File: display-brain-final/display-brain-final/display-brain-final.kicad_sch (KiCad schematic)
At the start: 25 parts, among them J1 Conn_01x02_Socket, J2 Conn_01x05_Socket, J3 Conn_01x19_Socket, J4 Conn_01x19_Socket, J5 Conn_01x04_Socket, J6 Conn_01x05_Socket, J7 Conn_01x02_Socket, P1 USB_C_Plug_USB2.0, U2 ESP32-WROOM-32, U3 LM317_TO-252

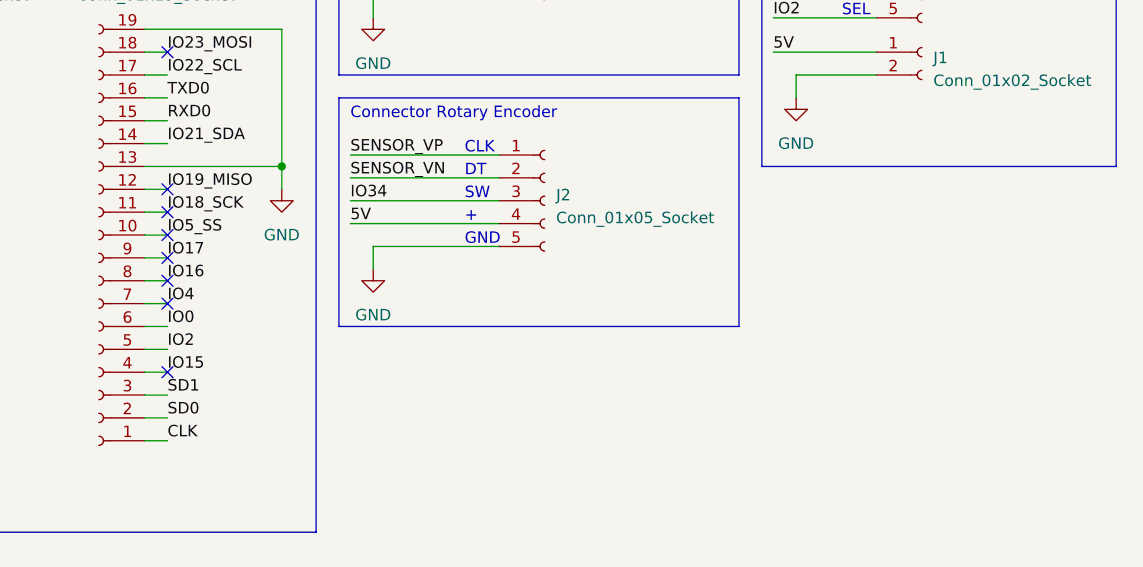
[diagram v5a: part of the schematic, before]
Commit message: display and funk changed
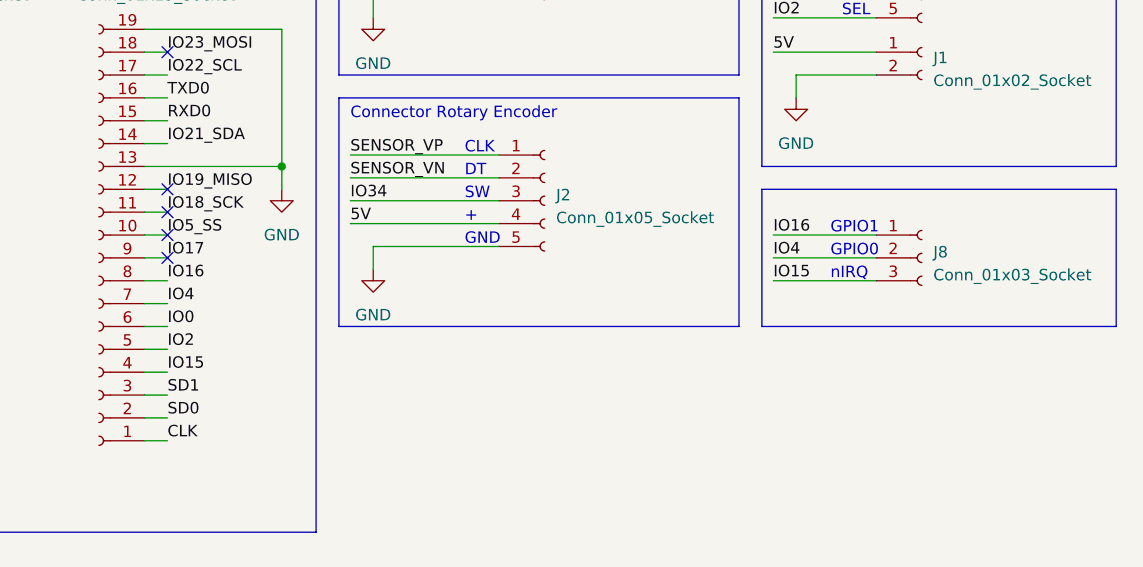
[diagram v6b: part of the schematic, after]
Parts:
- added J8: Conn_01x03_Socket, Connector_PinSocket_2.54mm:PinSocket_1x03_P2.54mm_Vertical, symbol Connector:Conn_01x03_Socket
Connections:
- net IO15: now also J8.3 (Pin_3)
- net IO16: now also J8.1 (Pin_1)
- net IO4: now also J8.2 (Pin_2)
- no-connect marks 29 -> 26
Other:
- note added: "GPIO0"
- note added: "GPIO1"
- note added: "nIRQ"
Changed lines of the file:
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@@
   (junction (at 144.78 163.83) (diameter 0) (color 0 0 0 0)
   )
-  (no_connect (at 127 59.69))
   (no_connect (at 127 54.61))
   (no_connect (at 87.63 44.45))
@@
   (no_connect (at 69.85 142.24))
   (no_connect (at 127 57.15))
-  (no_connect (at 127 62.23))
   (no_connect (at 127 49.53))
   (no_connect (at 87.63 62.23))
@@
   (no_connect (at 87.63 69.85))
   (no_connect (at 96.52 102.87))
-  (no_connect (at 127 69.85))
   (no_connect (at 83.82 102.87))
   (no_connect (at 123.19 102.87))
@@
     (stroke (width 0) (type default))
   )
+  (polyline (pts (xy 193.04 64.77) (xy 232.41 64.77))
+    (stroke (width 0) (type default))
+  )
   (wire (pts (xy 194.31 20.32) (xy 205.74 20.32))
     (stroke (width 0) (type default))
@@
     (stroke (width 0) (type default))
   )
+  (polyline (pts (xy 232.41 64.77) (xy 232.41 49.53))
+    (stroke (width 0) (type default))
+  )
   (wire (pts (xy 124.46 34.29) (xy 127 34.29))
     (stroke (width 0) (type default))
@@
     (stroke (width 0) (type default))
   )
+  (polyline (pts (xy 232.41 49.53) (xy 193.04 49.53))
+    (stroke (width 0) (type default))
+  )
   (wire (pts (xy 87.63 46.99) (xy 100.33 46.99))
     (stroke (width 0) (type default))
   )
+  (polyline (pts (xy 193.04 49.53) (xy 193.04 64.77))
+    (stroke (width 0) (type default))
+  )
   (wire (pts (xy 19.05 124.46) (xy 19.05 129.54))
     (stroke (width 0) (type default))
@@
     (stroke (width 0) (type default))
   )
+  (wire (pts (xy 194.31 54.61) (xy 205.74 54.61))
+    (stroke (width 0) (type default))
+  )
   (wire (pts (xy 59.69 34.29) (xy 66.04 34.29))
     (stroke (width 0) (type default))
@@
     (stroke (width 0) (type default))
   )
+  (wire (pts (xy 194.31 59.69) (xy 205.74 59.69))
+    (stroke (width 0) (type default))
+  )
   (wire (pts (xy 147.32 48.26) (xy 163.83 48.26))
     (stroke (width 0) (type default))
@@
     (stroke (width 0) (type default))
   )
+  (wire (pts (xy 194.31 57.15) (xy 205.74 57.15))
+    (stroke (width 0) (type default))
+  )
   (polyline (pts (xy 135.89 104.14) (xy 81.28 104.14))
     (stroke (width 0) (type default))
@@
     (effects (font (size 1.27 1.27)) (justify left bottom))
   )
+  (text "GPIO1" (at 200.66 54.61 0)
+    (effects (font (size 1.27 1.27)) (justify left bottom))
+  )
   (text "GND" (at 160.02 55.88 0)
     (effects (font (size 1.27 1.27)) (justify left bottom))
@@
   )
   (text "Power Connector" (at 15.24 111.76 0)
+    (effects (font (size 1.27 1.27)) (justify left bottom))
+  )
+  (text "GPIO0" (at 200.66 57.15 0)
+    (effects (font (size 1.27 1.27)) (justify left bottom))
+  )
+  (text "nIRQ" (at 200.66 59.69 0)
     (effects (font (size 1.27 1.27)) (justify left bottom))
   )
@@
     (effects (font (size 1.27 1.27)) (justify left bottom))
   )
+  (label "IO4" (at 194.31 57.15 0) (fields_autoplaced)
+    (effects (font (size 1.27 1.27)) (justify left bottom))
+  )
   (label "IO34" (at 147.32 50.8 0) (fields_autoplaced)
     (effects (font (size 1.27 1.27)) (justify left bottom))
@@
     (effects (font (size 1.27 1.27)) (justify left bottom))
   )
+  (label "IO16" (at 194.31 54.61 0) (fields_autoplaced)
+    (effects (font (size 1.27 1.27)) (justify left bottom))
+  )
   (label "CLK" (at 22.86 69.85 0) (fields_autoplaced)
     (effects (font (size 1.27 1.27)) (justify left bottom))
@@
   )
   (label "IO33" (at 66.04 82.55 0) (fields_autoplaced)
+    (effects (font (size 1.27 1.27)) (justify left bottom))
+  )
+  (label "IO15" (at 194.31 59.69 0) (fields_autoplaced)
     (effects (font (size 1.27 1.27)) (justify left bottom))
   )
@@
         )
       )
+    )
+  )
+  (symbol (lib_id "Connector:Conn_01x03_Socket") (at 210.82 57.15 0) (unit 1)
+    (in_bom yes) (on_board yes) (dnp no) (fields_autoplaced)
+    (property "Reference" "J8" (at 212.09 56.515 0)
+      (effects (font (size 1.27 1.27)) (justify left))
+    )
+    (property "Value" "Conn_01x03_Socket" (at 212.09 59.055 0)
+      (effects (font (size 1.27 1.27)) (justify left))
+    )
+    (property "Footprint" "Connector_PinSocket_2.54mm:PinSocket_1x03_P2.54mm_Vertical" (at 210.82 57.15 0)
+      (effects (font (size 1.27 1.27)) hide)
+    )
+    (property "Datasheet" "~" (at 210.82 57.15 0)
+      (effects (font (size 1.27 1.27)) hide)
+    )
+    (pin "1")
+    (pin "2")
+    (pin "3")
+    (instances
+      (project "display-brain-final"
+        (path "/574a6960-c63c-4761-9f4b-096834c9b760"
+          (reference "J8") (unit 1)
+        )
+      )
